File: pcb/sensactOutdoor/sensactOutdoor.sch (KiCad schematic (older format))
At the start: 121 parts, among them J1 48V, J10 CAN, J11 EXT2, J12 CAN, J13 RGB, J14 N1, J15 N2, J2 Conn_01x03, J3 Conn_01x03, J4 PROG, J5 LED CC, J6 PWM_OUT, J7 EXT1, J8 PWM_OUT, J9 230V, K1 ALDP105W, K2 ALDP105W, K3 ALDP105W, K4 ALDP105W, K5 ALDP105W, K6 ALDP105W, Q1 N, Q10 BC847, Q11 BC847, Q2 N, Q3 N, Q4 N, Q5 N, Q6 BC847, Q7 BC847, Q8 BC847, Q9 BC847, SW1 TERM ON OFF, U1 ESP32-WROOM-32U, U2 A6211, U3 LMR16006X, U4 SN65HVD230, U5 AMS1117-3.3, U6 RF, U7 RX470B, U8 EL814

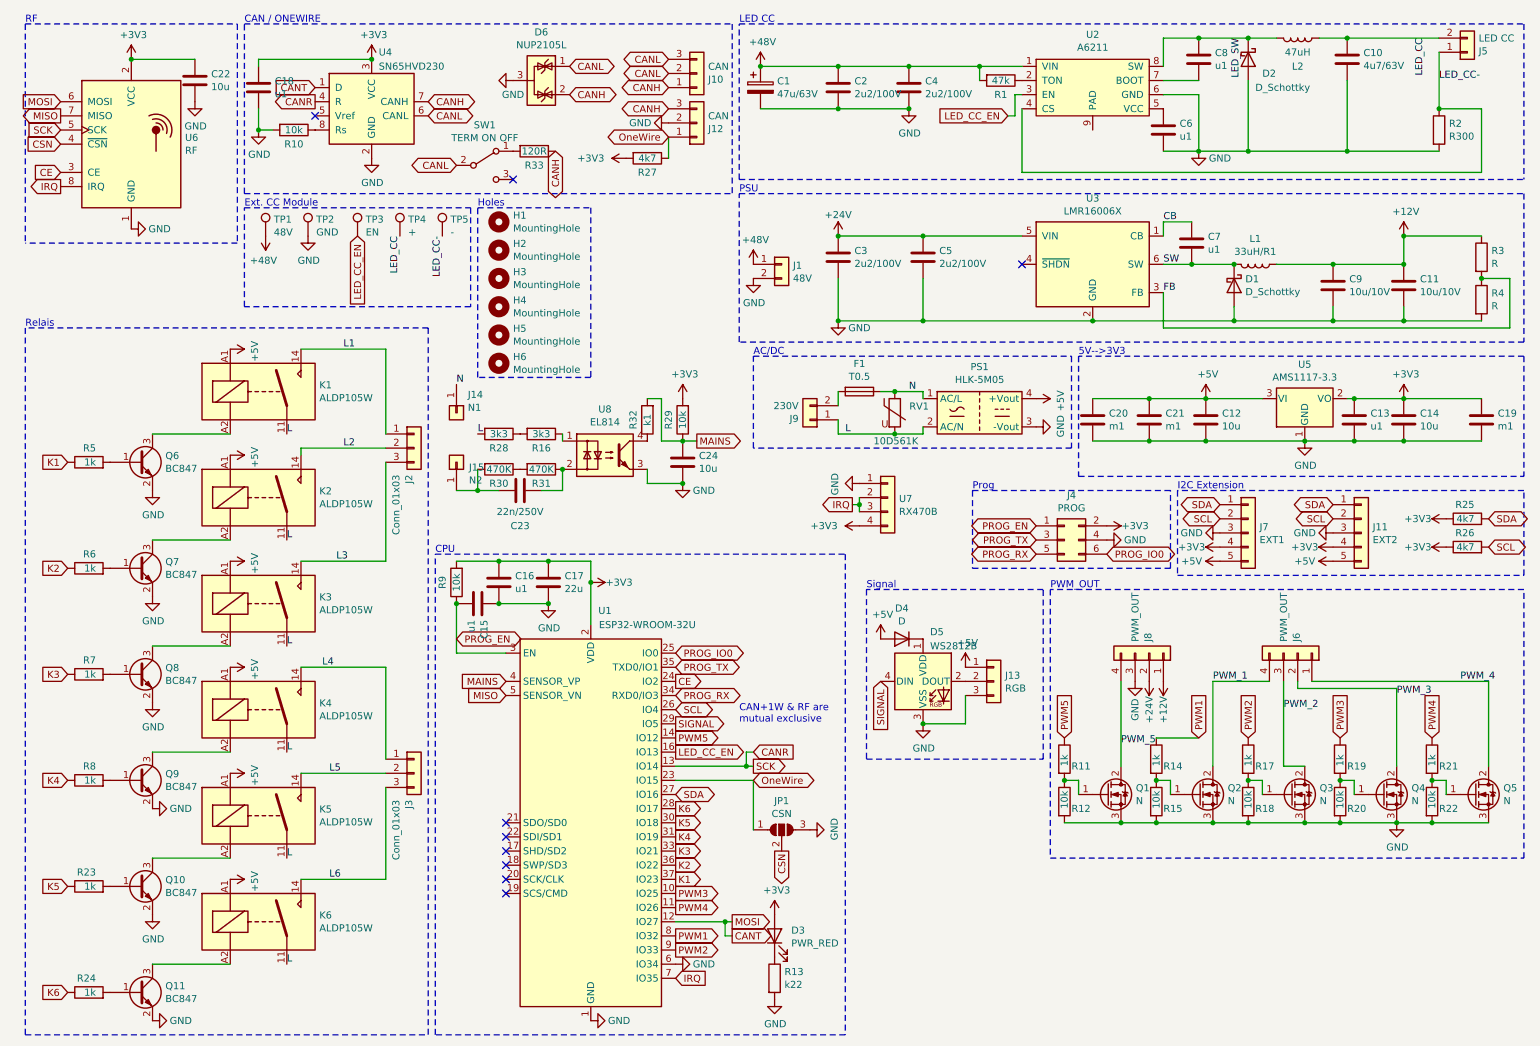
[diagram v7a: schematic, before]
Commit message: Improvements in pcb design of sensactOutdoor and sensactHsIO4
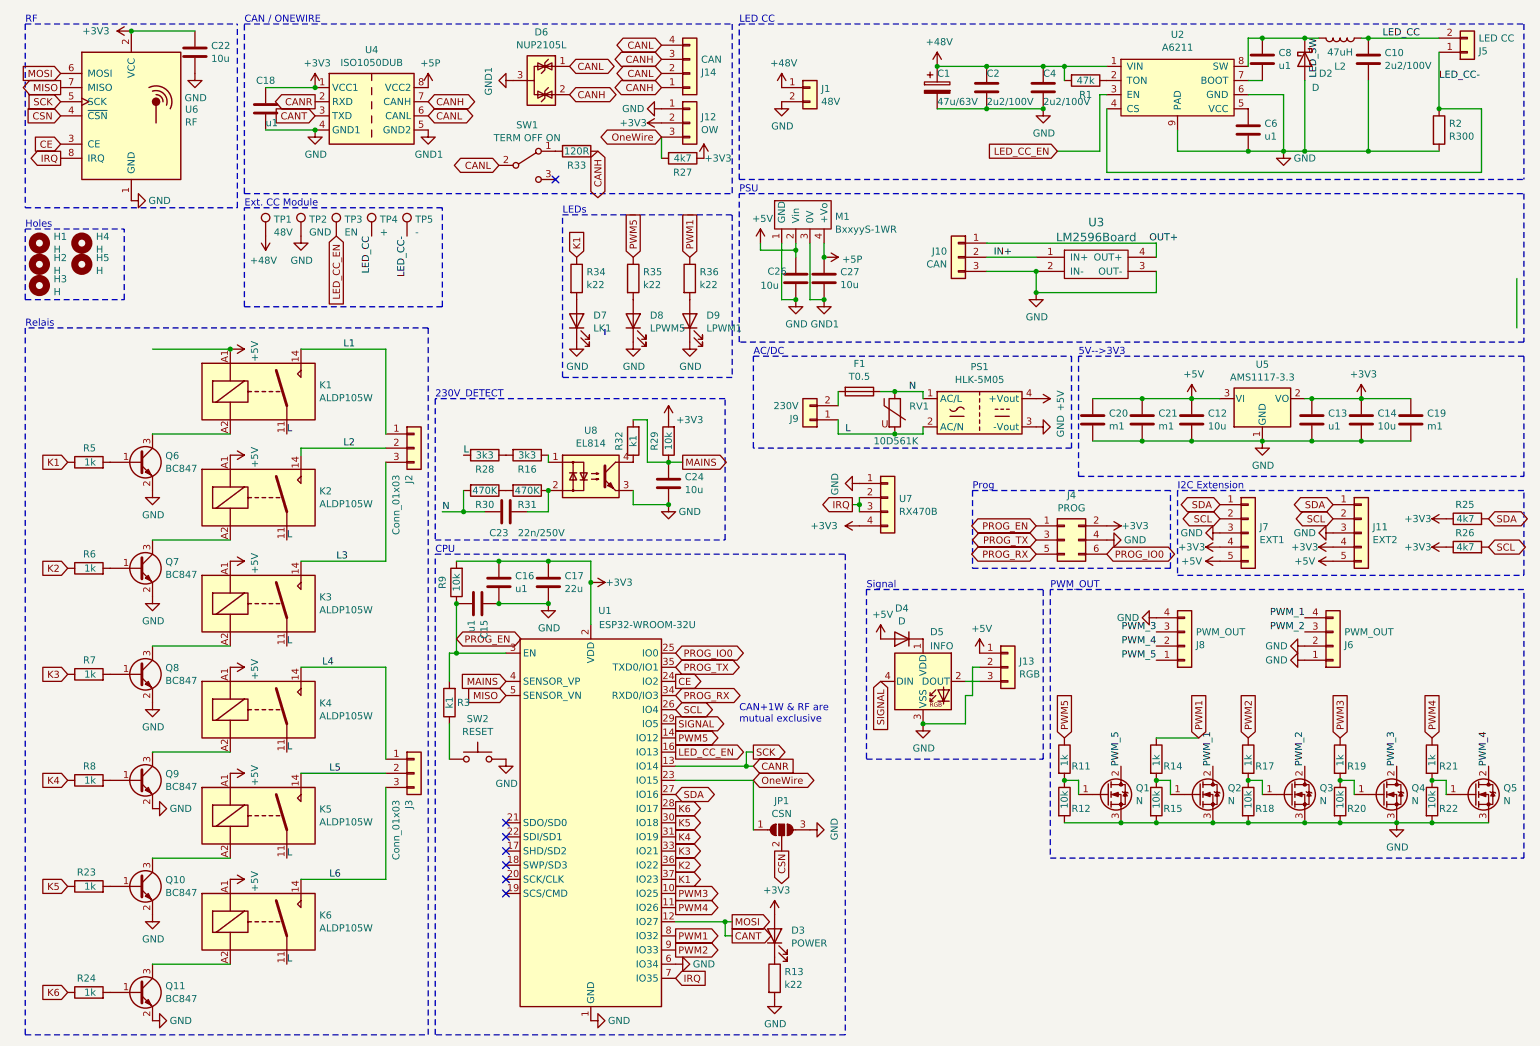
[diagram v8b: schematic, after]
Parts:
- removed C11, C9: 10u/10V, Capacitor_SMD:C_1206_3216Metric_Pad1.33x1.80mm_HandSolder, symbol Device:C
- removed C3, C5: 2u2/100V, Capacitor_SMD:C_1812_4532Metric_Pad1.57x3.40mm_HandSolder, symbol Device:C
- removed C7: u1, Capacitor_SMD:C_0805_2012Metric_Pad1.18x1.45mm_HandSolder, symbol Device:C
- removed D1: D_Schottky, Diode_SMD:D_SMA_Handsoldering, symbol Device:D_Schottky
- removed H6: MountingHole, MountingHole:MountingHole_3.2mm_M3, symbol Mechanical:MountingHole
- removed J14: N1, liebler_CONN:SolderWirePad_1x01_SMD_2x4mm, symbol Connector_Generic:Conn_01x01
- removed J15: N2, liebler_CONN:SolderWirePad_1x01_SMD_2x4mm, symbol Connector_Generic:Conn_01x01
- removed L1: 33uH/R1, sensact:L_7.3x7.3_H4.5_handsolder, symbol Device:L
- removed R10: 10k, Resistor_SMD:R_0805_2012Metric_Pad1.20x1.40mm_HandSolder, symbol Device:R
- removed R4: R, Resistor_SMD:R_0805_2012Metric_Pad1.20x1.40mm_HandSolder, symbol Device:R
- removed U3: LMR16006X, Package_TO_SOT_SMD:SOT-23-6, symbol Regulator_Switching:LMR16006YQ
- removed U4: SN65HVD230, sensact:SOIC-8_3.9x4.9mm_Pitch1.27mm_handsolder, symbol Interface_CAN_LIN:SN65HVD230
- added C26, C27: 10u, Capacitor_SMD:C_1206_3216Metric_Pad1.33x1.80mm_HandSolder, symbol Device:C
- added D7: LK1, LED_SMD:LED_0805_2012Metric_Pad1.15x1.40mm_HandSolder, symbol Device:LED
- added D8: LPWM5, LED_SMD:LED_0805_2012Metric_Pad1.15x1.40mm_HandSolder, symbol Device:LED
- added D9: LPWM1, LED_SMD:LED_0805_2012Metric_Pad1.15x1.40mm_HandSolder, symbol Device:LED
- added J14: CAN, Connector_Phoenix_MC:PhoenixContact_MCV_1,5_4-G-3.5_1x04_P3.50mm_Vertical, symbol Connector_Generic:Conn_01x04
- added M1: BxxyyS-1WR, liebler_MODULES:BxxxxS-1W, symbol liebler_MODULES:BxxyyS-1WR
- added R34, R35, R36: k22, Resistor_SMD:R_0805_2012Metric_Pad1.20x1.40mm_HandSolder, symbol Device:R
- added SW2: RESET, liebler_MECH:SW_Push_1P1T_NO_6x6mm_H9.5mm, symbol Switch:SW_Push
- added U3: LM2596Board, liebler_MODULES:LM2596HV, symbol sensact:LM2596Board
- added U4: ISO1050DUB, liebler_SEMICONDUCTORS:SOP-8_6.62x9.15mm_P2.54mm_handsolder, symbol Interface_CAN_LIN:ISO1050DUB
- C10: value 4u7/63V -> 2u2/100V
- D2: value D_Schottky -> D
- D3: value PWR_RED -> POWER
- D5: value WS2812B -> INFO; footprint sensact:PLCC4-5050 -> liebler_SEMICONDUCTORS:WS2812b_handsolder
- H1, H2, H3, H4, H5: value MountingHole -> H
- J12: value CAN -> OW
- J4: footprint Connector_IDC:IDC-Header_2x03_P2.54mm_Vertical -> liebler_CONN:IDC_2x03_P1.27mm_Vertical
- R3: value R -> k1
- RV1: footprint Varistor:RV_Disc_D12mm_W6.1mm_P7.5mm -> Varistor:RV_Disc_D12mm_W3.9mm_P7.5mm
- SW1: value TERM ON OFF -> TERM OFF ON; footprint liebler_MECH:SW_SPDT_PCM12_handsolder -> liebler_MECH:SS12D00
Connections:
- net +24V is gone; now on net PWM_4: J8.2 (Pin_2)
- net FB is gone; now on net PROG_EN: R3.2
- net +3V3: now also J12.2 (Pin_2), R27.1, U4.1 (VCC1); no longer R27.2
- net +5V: now also C26.1, M1.2 (Vin)
- net CANH: now also J14.1 (Pin_1), J14.3 (Pin_3), U4.7 (CANH); no longer J10.1 (Pin_1), J12.3 (Pin_3)
- net CANL: now also J14.2 (Pin_2), J14.4 (Pin_4), U4.6 (CANL); no longer J10.2 (Pin_2), J10.3 (Pin_3)
- net CANR: now also U4.2 (RXD)
- net CANT: now also U4.3 (TXD)
- net GND: now also J10.3 (Pin_3), J12.1 (Pin_1), J13.2 (Pin_2), J6.1 (Pin_1), J6.2 (Pin_2), J8.4 (Pin_4), U2.9 (PAD), C26.2, D7.1 (K), D8.1 (K), D9.1 (K), M1.1 (GND), SW2.2, U3.2 (IN-), U3.3 (OUT-), U4.4 (GND1); no longer D6.3 (A), J12.2 (Pin_2), J13.3 (Pin_3), J8.3 (Pin_3)
- net K1: now also R34.1
- net N: now also C23.1, R30.2
- net OneWire: now also J12.3 (Pin_3), R27.2; no longer J12.1 (Pin_1), R27.1
- net PWM1: now also R36.1
- net PWM5: now also R35.1
- net PWM_3: now also J8.3 (Pin_3); no longer J6.2 (Pin_2)
- net PWM_4: no longer J6.1 (Pin_1)
- net PWM_5: now also J8.1 (Pin_1); no longer J8.4 (Pin_4)
- net at D5.2 (DOUT): now also J13.3 (Pin_3); no longer J13.2 (Pin_2)
- net +12V: no longer names the net of R3.1
- net +12V: now also SW2.1; no longer J8.1 (Pin_1)
- new net: D7.2 (A), R34.2
- new net: D8.2 (A), R35.2
- new net: D9.2 (A), R36.2
- new net +5P: C27.1, M1.4 (+Vo), U4.8 (VCC2)
- new net GND1: C27.2, D6.3 (A), M1.3 (0V), U4.5 (GND2)
- new net IN+: J10.2 (Pin_2), U3.1 (IN+)
- new net OUT+: J10.1 (Pin_1), U3.4 (OUT+)
- no-connect marks 9 -> 7
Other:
- note added: "230V_DETECT"
- note added: "LEDs"
- moved on the sheet: C1, C10, C12, C13, C14, C18, C19, C2, C21, C22, C23, C24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
